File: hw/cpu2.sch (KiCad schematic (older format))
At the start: 0 parts

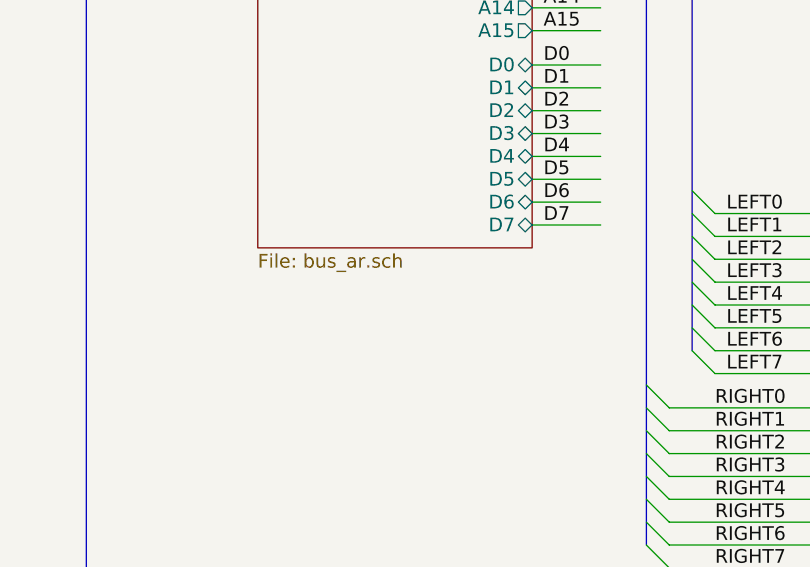
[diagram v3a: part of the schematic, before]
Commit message: specify prefix for bus_ar module
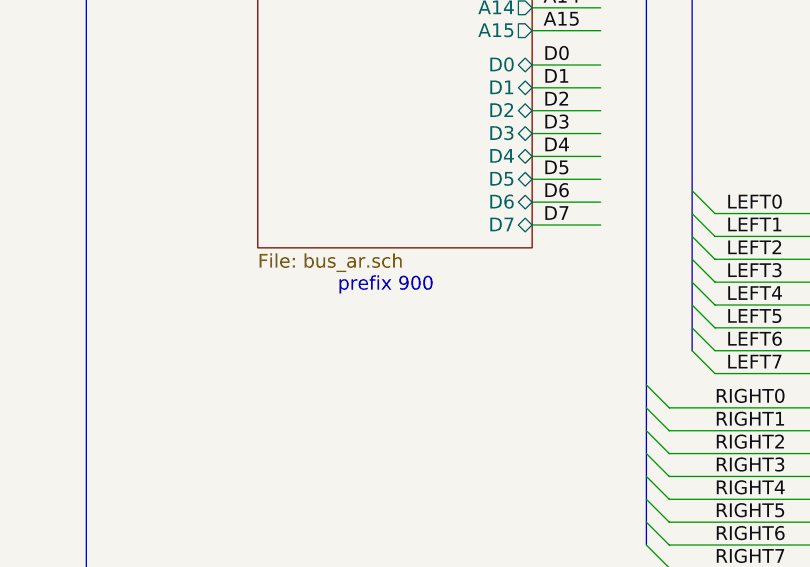
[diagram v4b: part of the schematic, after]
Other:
- note added: "prefix 900"
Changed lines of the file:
@@
 Text Label 7950 3600 0    60   ~ 0
 -COUT
+Text Notes 6200 12400 0    60   ~ 0
+prefix 900
 $EndSCHEMATC

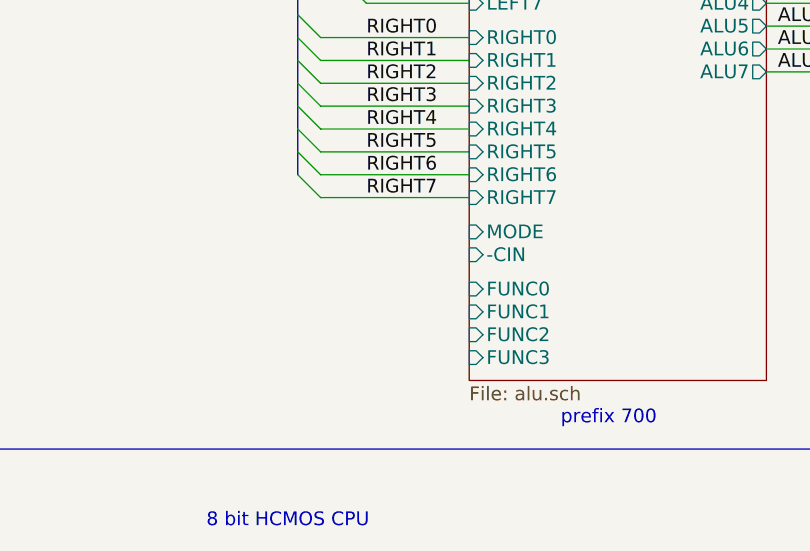
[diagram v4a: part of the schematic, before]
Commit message: added missing ALU inputs from microcode
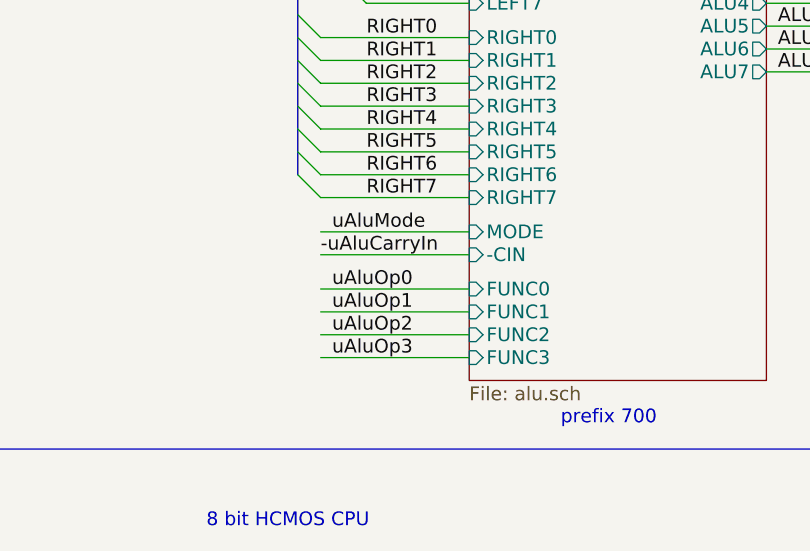
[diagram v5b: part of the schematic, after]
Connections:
- wire segments 223 -> 229
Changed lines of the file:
@@
 Text Notes 6200 12400 0    60   ~ 0
 prefix 900
+Wire Wire Line
+	8300 14000 7650 14000
+Wire Wire Line
+	8300 14100 7650 14100
+Wire Wire Line
+	8300 14200 7650 14200
+Wire Wire Line
+	8300 14300 7650 14300
+Text Label 7700 14000 0    60   ~ 0
+uAluOp0
+Text Label 7700 14100 0    60   ~ 0
+uAluOp1
+Text Label 7700 14200 0    60   ~ 0
+uAluOp2
+Text Label 7700 14300 0    60   ~ 0
+uAluOp3
+Wire Wire Line
+	8300 13750 7650 13750
+Wire Wire Line
+	8300 13850 7650 13850
+Text Label 7700 13750 0    60   ~ 0
+uAluMode
+Text Label 7650 13850 0    60   ~ 0
+-uAluCarryIn
 $EndSCHEMATC

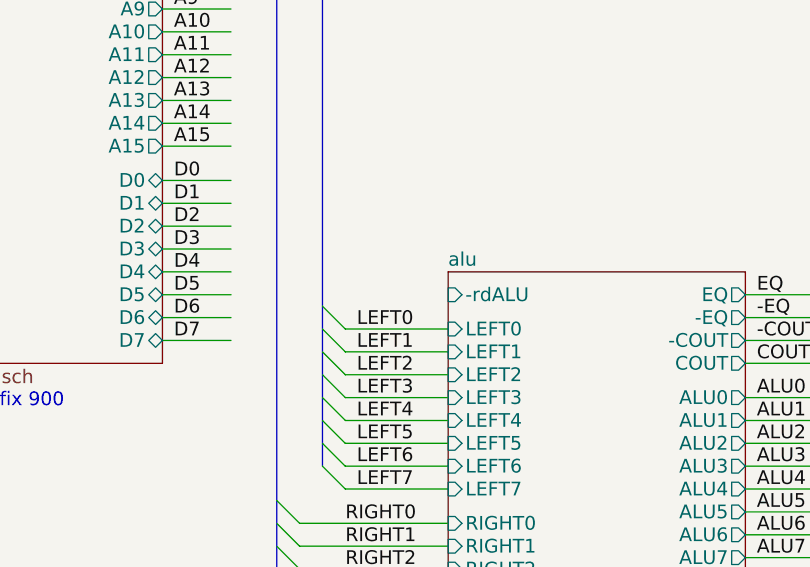
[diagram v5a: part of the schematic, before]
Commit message: connected one more ALU input signal
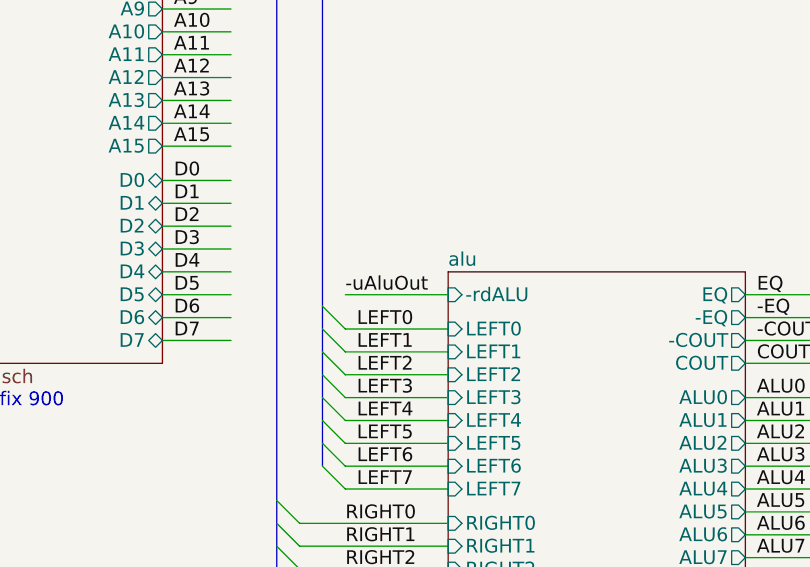
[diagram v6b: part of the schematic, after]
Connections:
- wire segments 229 -> 230
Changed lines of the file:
@@
 Text Label 7650 13850 0    60   ~ 0
 -uAluCarryIn
+Wire Wire Line
+	8300 11900 7850 11900
+Text Label 7850 11900 0    60   ~ 0
+-uAluOut
 $EndSCHEMATC

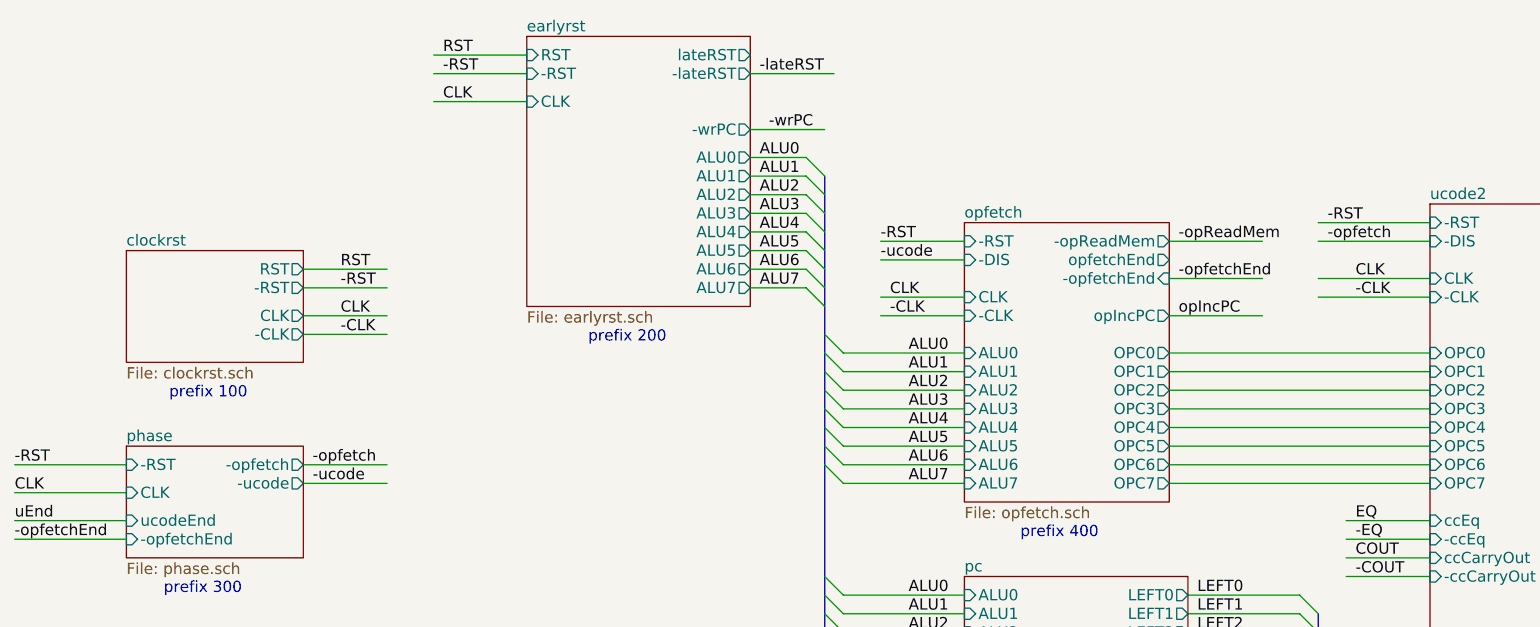
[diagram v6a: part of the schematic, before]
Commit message: use a buffer to replicate clock/reset signals
In particular, this allows us to limit the clock fan-out
to 8 inputs.
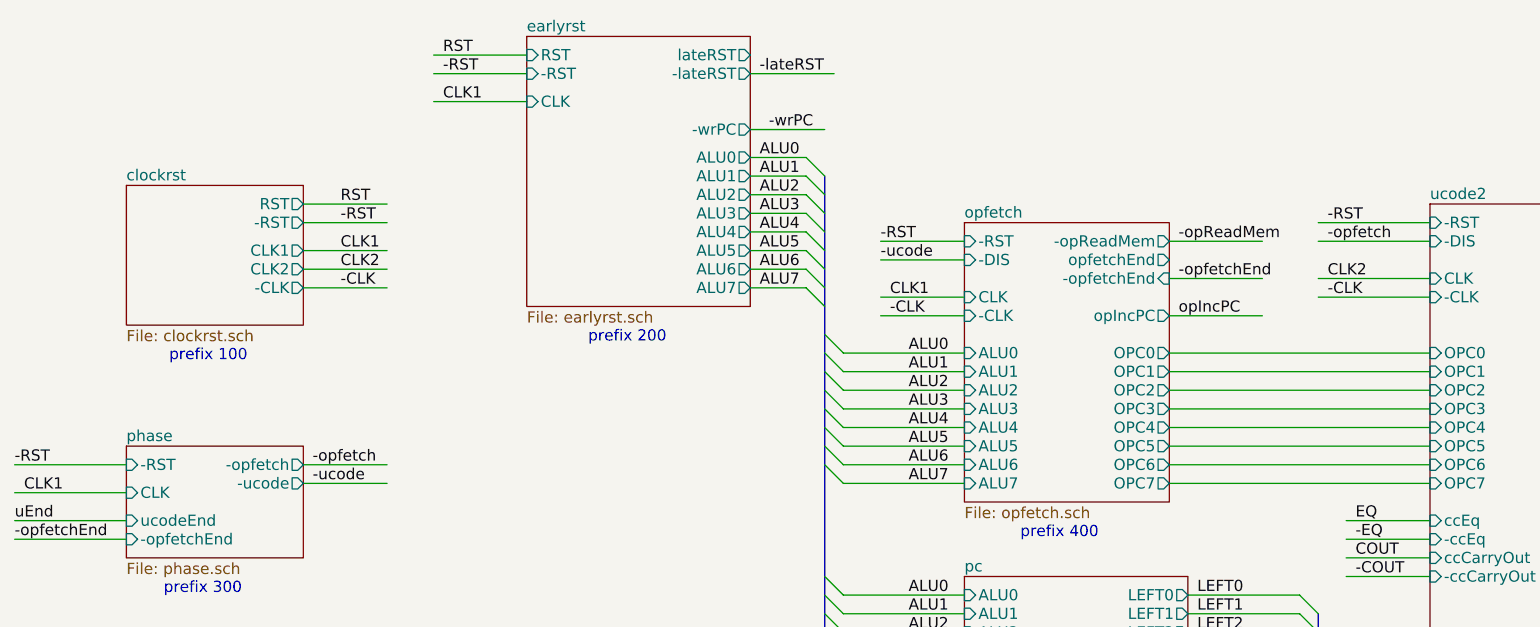
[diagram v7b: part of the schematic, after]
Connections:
- net labels added: CLK1, CLK2
- net labels removed: CLK
- wire segments 230 -> 231
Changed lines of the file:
@@
 $EndSheet
 $Sheet
-S 1350 1850 950  600
+S 1350 1500 950  750
 U 59395B62
 F0 "clockrst" 60
 F1 "clockrst.sch" 60
-F2 "CLK" O R 2300 2200 60
-F3 "-CLK" O R 2300 2300 60
-F4 "RST" O R 2300 1950 60
-F5 "-RST" O R 2300 2050 60
+F2 "CLK1" O R 2300 1850 60
+F3 "CLK2" O R 2300 1950 60
+F4 "-CLK" O R 2300 2050 60
+F5 "RST" O R 2300 1600 60
+F6 "-RST" O R 2300 1700 60
 $EndSheet
-Text Notes 2000 2650 2    60   ~ 0
+Text Notes 2000 2450 2    60   ~ 0
 prefix 100
 Text Notes 4250 2350 2    60   ~ 0
@@
 Wire Wire Line
 	7750 2100 8350 2100
-Text Label 7950 2100 0    60   ~ 0
+Text Label 7800 2100 0    60   ~ 0
 -CLK
 Wire Wire Line
@@
 -opReadMem
 Wire Wire Line
-	2300 1950 2750 1950
+	2300 1600 2750 1600
+Wire Wire Line
+	2300 1700 2750 1700
+Wire Wire Line
+	2300 1850 2750 1850
 Wire Wire Line
 	2300 2050 2750 2050
-Wire Wire Line
-	2300 2200 2750 2200
-Wire Wire Line
-	2300 2300 2750 2300
-Text Label 2500 1950 0    60   ~ 0
+Text Label 2500 1600 0    60   ~ 0
 RST
+Text Label 2500 1700 0    60   ~ 0
+-RST
 Text Label 2500 2050 0    60   ~ 0
--RST
-Text Label 2500 2200 0    60   ~ 0
-CLK
-Text Label 2500 2300 0    60   ~ 0
 -CLK
 Text Label 4750 900  0    60   ~ 0
 -lateRST
-Text Label 750  3150 0    60   ~ 0
-CLK
 Text Label 750  3000 0    60   ~ 0
 -RST
@@
 Wire Wire Line
 	5850 2200 5400 2200
-Text Label 5450 2100 0    60   ~ 0
-CLK
 Text Label 5450 2200 0    60   ~ 0
 -CLK
@@
 Text Label 7000 2000 0    60   ~ 0
 -opfetchEnd
-Text Label 7950 2000 0    60   ~ 0
-CLK
 Text Label 7800 1800 0    60   ~ 0
 -opfetch
@@
 Text Label 3050 900  0    60   ~ 0
 -RST
-Text Label 3050 1050 0    60   ~ 0
-CLK
 Wire Wire Line
 	9700 1700 10250 1700
@@
 Text Label 7850 11900 0    60   ~ 0
 -uAluOut
+Wire Wire Line
+	2300 1950 2750 1950
+Text Label 2500 1850 0    60   ~ 0
+CLK1
+Text Label 2500 1950 0    60   ~ 0
+CLK2
+Text Label 800  3150 0    60   ~ 0
+CLK1
+Text Label 3050 1050 0    60   ~ 0
+CLK1
+Text Label 7800 2000 0    60   ~ 0
+CLK2
+Text Label 5450 2100 0    60   ~ 0
+CLK1
 $EndSCHEMATC
